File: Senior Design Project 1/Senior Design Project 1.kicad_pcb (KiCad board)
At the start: 2 copper layers, 32 parts, among them U2 74HC273, U3 LM393NG, U6 LM555xN, U9 74HC273

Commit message: Updated Schematic & PCB
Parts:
- removed REF**: TerminalBlock_4Ucon_1x02_P3.50mm_Vertical, TerminalBlock_4Ucon:TerminalBlock_4Ucon_1x02_P3.50mm_Vertical
- removed REF**: TerminalBlock_4Ucon_1x03_P3.50mm_Vertical, TerminalBlock_4Ucon:TerminalBlock_4Ucon_1x03_P3.50mm_Vertical
- added 9V: TerminalBlock_4Ucon_1x02_P3.50mm_Vertical, TerminalBlock_4Ucon:TerminalBlock_4Ucon_1x02_P3.50mm_Vertical, F.Cu at (115.0, 22.8)
- added V1: 5V, TerminalBlock:TerminalBlock_bornier-3_P5.08mm, F.Cu at (22.7, 75.4)
- moved R15 59.0 mm to (118.1, 110.2), turned to 180 degrees
- moved R14 57.3 mm to (118.1, 105.0), turned to 180 degrees
- moved R13 55.7 mm to (118.1, 99.9), turned to 180 degrees
- moved R12 54.0 mm to (118.3, 94.7), turned to 180 degrees
- moved U9 50.9 mm to (157.4, 112.5)
- moved R11 46.9 mm to (165.4, 88.6), turned to 90 degrees
- moved D4 46.5 mm to (127.7, 110.3), turned to 90 degrees
- moved R8 44.6 mm to (165.4, 74.3), turned to 90 degrees
- moved R6 42.1 mm to (165.4, 61.3), turned to 90 degrees
- moved R10 42.0 mm to (165.4, 48.2), turned to 90 degrees
- moved Hex Inverter 41.3 mm to (50.6, 59.5)
- moved D3 38.6 mm to (127.7, 105.1), turned to 90 degrees
- moved D2 30.7 mm to (127.7, 99.9), turned to 90 degrees
- moved R9 30.2 mm to (150.6, 74.2)
- moved R7 26.9 mm to (150.4, 61.2)
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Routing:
- net GND: track 0.00 -> 126.8 mm
- net Net-(U6-THR): track 0.00 -> 39.6 mm
- net Net-(D2-A): track 0.00 -> 23.1 mm
- net Net-(D4-A): track 0.00 -> 23.0 mm
- net Net-(D3-A): track 0.00 -> 22.5 mm
- net Net-(D1-A): track 0.00 -> 22.1 mm
- net Net-(U6-DIS): track 0.00 -> 21.3 mm
- net Net-(R11-Pad2): track 0.00 -> 13.8 mm
- net Net-(R6-Pad1): track 0.00 -> 12.8 mm
- net Net-(R10-Pad1): track 0.00 -> 12.2 mm
- net VDD: track 0.00 -> 11.9 mm
- net Net-(D1-K): track 0.00 -> 9.82 mm
- net Net-(D2-K): track 0.00 -> 9.77 mm
- net Net-(D4-K): track 0.00 -> 9.66 mm
- net Net-(D3-K): track 0.00 -> 9.61 mm
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
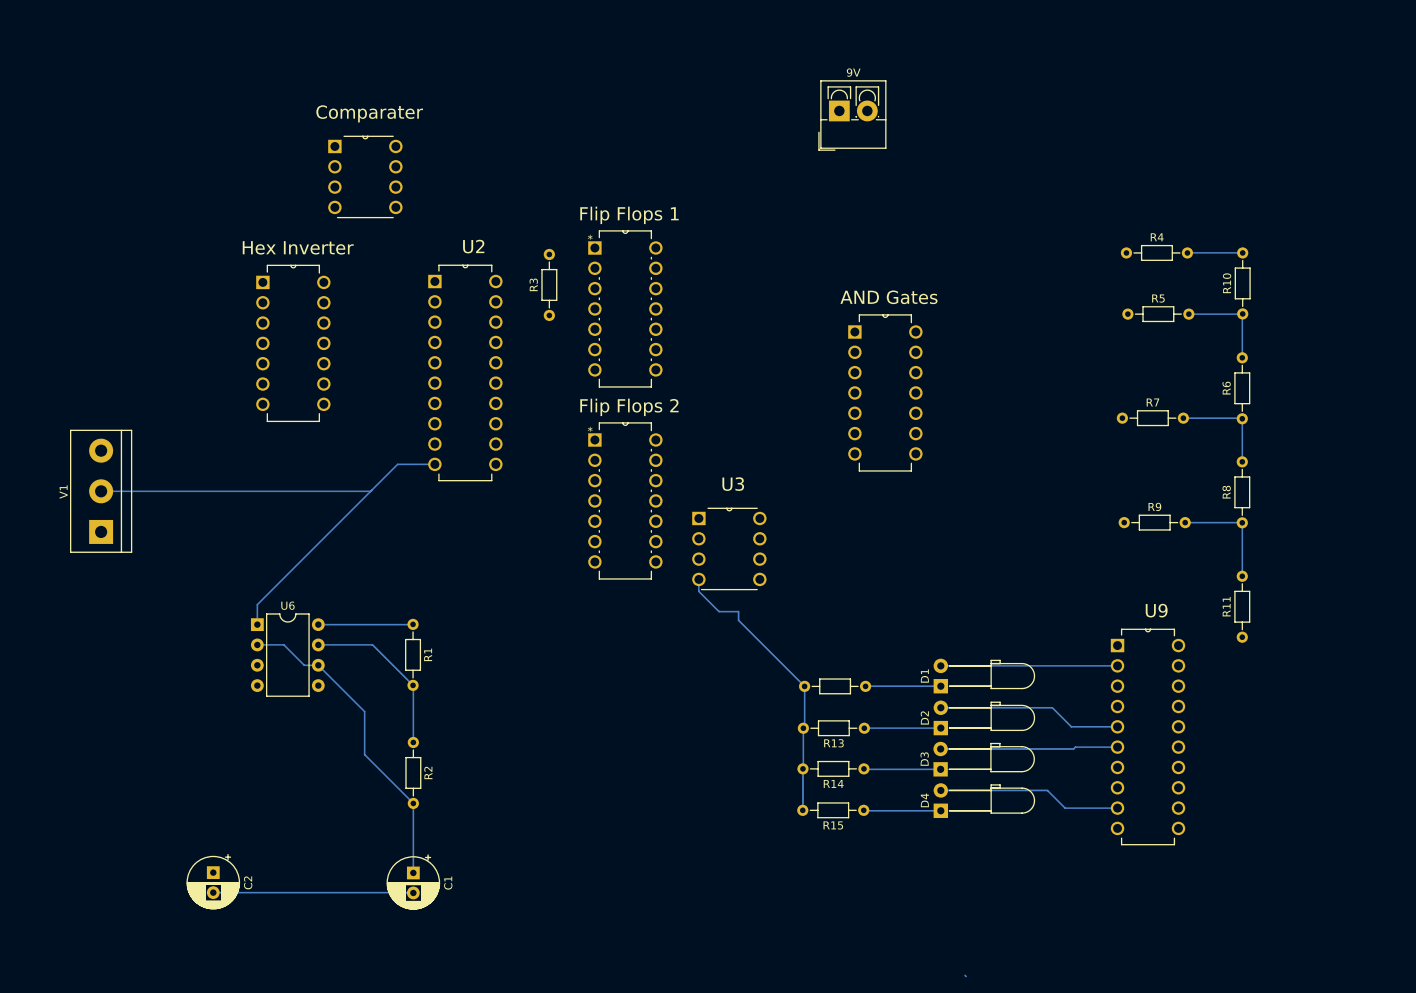
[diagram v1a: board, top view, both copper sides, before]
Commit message: Footprint fixes and updated PCB design
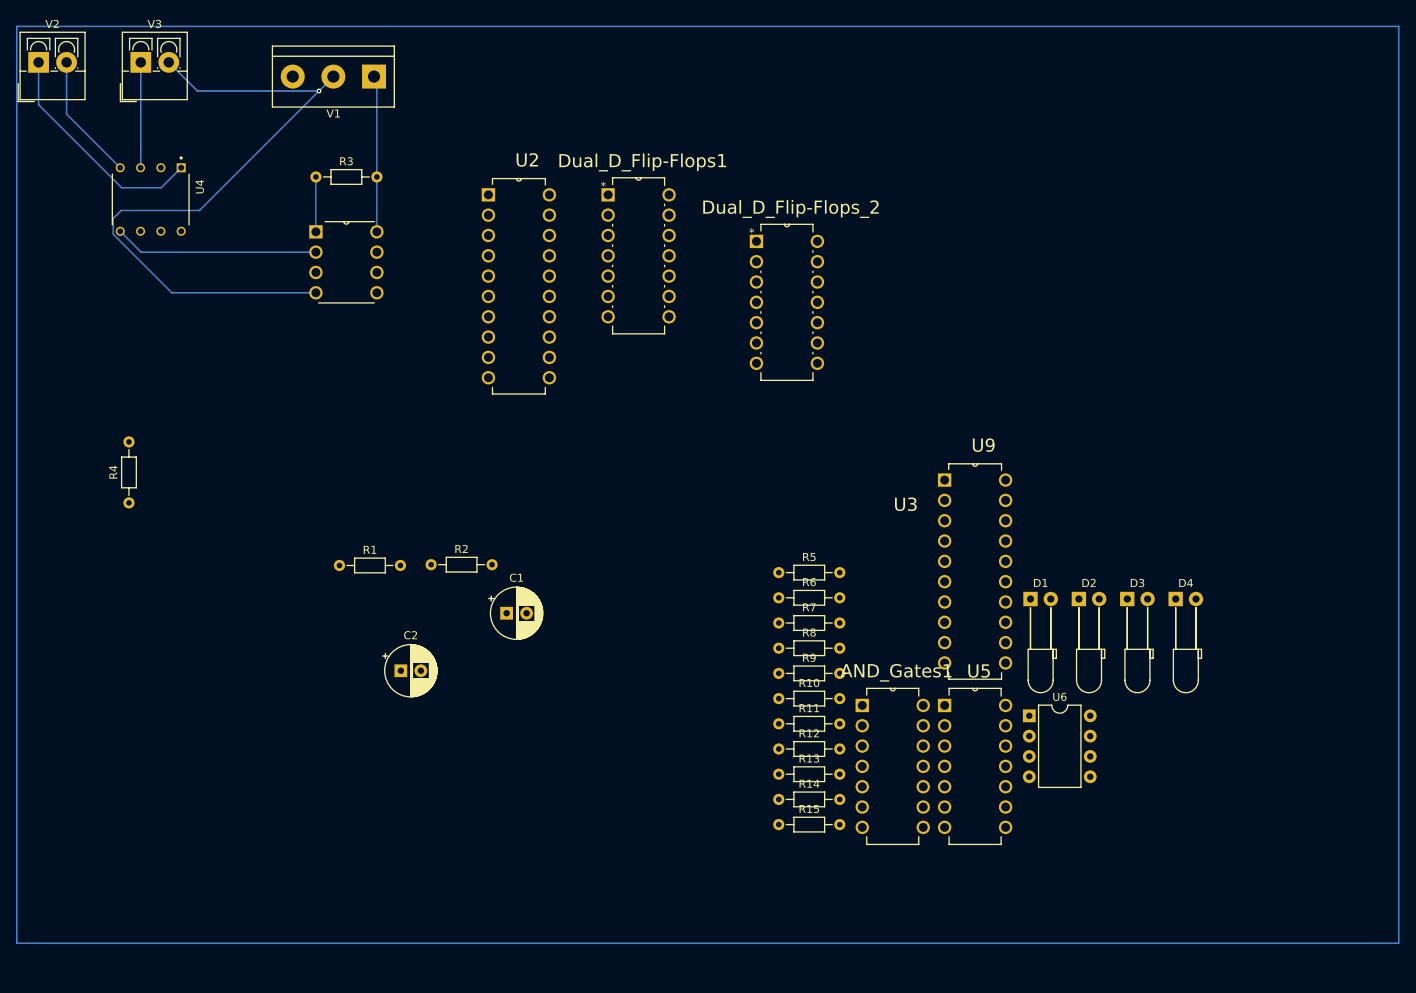
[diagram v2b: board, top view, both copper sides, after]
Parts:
- removed 9V: TerminalBlock_4Ucon_1x02_P3.50mm_Vertical, TerminalBlock_4Ucon:TerminalBlock_4Ucon_1x02_P3.50mm_Vertical
- removed AND Gates: DIP254P762X420-14, DIP254P762X420-14
- removed Comparater: DIP254P762X533-8, LM393NG:DIP254P762X533-8
- removed Flip Flops 1: DIP254P762X420-14, 74HC74N Library:DIP254P762X420-14
- removed Flip Flops 2: DIP254P762X420-14, 74HC74N Library:DIP254P762X420-14
- removed Hex Inverter: DIP254P762X420-14, DIP254P762X420-14
- added AND_Gates1: 74HC08N, 74HC08N Library:DIP254P762X420-14, F.Cu at (125.5, 112.3)
- added Dual_D_Flip-Flops1: 74HC74N_652, 74HC74N Library:DIP254P762X420-14, F.Cu at (93.7, 48.5)
- added Dual_D_Flip-Flops_2: 74HC74N_652, 74HC74N Library:DIP254P762X420-14, F.Cu at (112.3, 54.3)
- added U4: LF398N_NOPB, LF398N:DIP794W45P254L959H508Q8, F.Cu at (28.9, 33.9)
- added U5: 74AHC04, 74HC04N:DIP254P762X420-14, F.Cu at (135.8, 112.3)
- added V2: 9, TerminalBlock_4Ucon:TerminalBlock_4Ucon_1x02_P3.50mm_Vertical, F.Cu at (14.9, 16.7)
- added V3: 3, TerminalBlock_4Ucon:TerminalBlock_4Ucon_1x02_P3.50mm_Vertical, F.Cu at (27.7, 16.7)
- moved R4 128.5 mm to (26.2, 71.8), turned to 90 degrees
- moved U6 97.2 mm to (138.8, 98.4)
- moved R10 75.3 mm to (107.5, 96.2), turned to 0 degrees
- moved V1 66.4 mm to (56.9, 18.5), turned to 180 degrees
- moved R6 62.1 mm to (107.5, 83.6), turned to 0 degrees
- moved R8 60.0 mm to (107.5, 89.9), turned to 0 degrees
- moved U3 59.8 mm to (57.2, 45.5)
- moved R11 58.9 mm to (107.5, 99.4), turned to 0 degrees
- moved R5 54.3 mm to (107.5, 80.5)
- moved R7 50.0 mm to (107.5, 86.8)
- moved R9 47.1 mm to (107.5, 93.1)
- moved D4 39.5 mm to (157.1, 83.8), turned to 0 degrees
- moved C1 34.5 mm to (73.4, 85.6), turned to 0 degrees
- moved C2 34.4 mm to (60.2, 92.8), turned to 0 degrees
- moved R3 33.9 mm to (49.6, 31.0), turned to 0 degrees
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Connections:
- R1 pad 1: VDD -> Net-(AND_Gates1-1A)
- R3 pad 2: VDD -> Net-(AND_Gates1-1A)
- U2 pad 20: +5V -> Net-(AND_Gates1-1A)
- U2 pad 3: VDD -> Net-(AND_Gates1-1A)
- U3 pad 2: +3V -> Net-(U3-IN_A)
- U3 pad 8: +5V -> Net-(AND_Gates1-1A)
- U6 pad 4: VDD -> Net-(AND_Gates1-1A)
- U6 pad 8: VDD -> Net-(AND_Gates1-1A)
- U9 pad 20: +5V -> Net-(AND_Gates1-1A)
- V1 pad 1: Net-(Dual_D_Flip-Flops1-VCC) -> Net-(AND_Gates1-1A)
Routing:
- net GND: track 126.8 -> 85.4 mm, vias 0 -> 1
- net Net-(U6-THR): track 39.6 -> 0.00 mm
- net Net-(U4-V+): track 0.00 -> 28.4 mm
- net Net-(U3-IN_A): track 0.00 -> 25.5 mm
- net Net-(D2-A): track 23.1 -> 0.00 mm
- net Net-(D4-A): track 23.0 -> 0.00 mm
- net Net-(D3-A): track 22.5 -> 0.00 mm
- net Net-(D1-A): track 22.1 -> 0.00 mm
- net Net-(U6-DIS): track 21.3 -> 0.00 mm
- net Net-(AND_Gates1-1A): track 0.00 -> 20.8 mm
- net Net-(U4-V-): track 0.00 -> 16.0 mm
- net Net-(R11-Pad2): track 13.8 -> 0.00 mm
- net Net-(U4-INPUT): track 0.00 -> 13.2 mm
- net Net-(R6-Pad1): track 12.8 -> 0.00 mm
- net Net-(R10-Pad1): track 12.2 -> 0.00 mm
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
